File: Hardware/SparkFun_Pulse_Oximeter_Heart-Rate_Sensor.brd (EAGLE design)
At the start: 25.4 x 12.7 mm, 48 parts, among them U1 MAX30101EFD+T, U2 MAX32664GWEA+T, U3 1.8V/100mA, Y1 32.768kHz

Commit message: Moves silk labels around
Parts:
- added U$17: (no value), Pulse:PULSE0
- added U$18: (no value), and:AND0
- added U$19: (no value), SparkFun-Aesthetics:SFE_LOGO_FLAME_.1
- moved U$16 9.56 mm to (19.6, 9.91)
- moved U$14 6.35 mm to (25.7, 10.9)
- moved U$15 6.35 mm to (25.7, 9.91)
- moved U$1 1.05 mm to (24.4, 8.38), turned to 270 degrees
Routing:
- net GND: vias 42 -> 40
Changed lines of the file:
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@@
 <element name="LOGO1" library="SparkFun-Aesthetics" package="SFE_LOGO_FLAME_.1" value="SFE_LOGO_FLAME.1_INCH" x="23.876" y="1.778" smashed="yes"/>
 <element name="LOGO2" library="SparkFun-Aesthetics" package="OSHW-LOGO-MINI" value="OSHW-LOGOMINI" x="21.082" y="1.524" smashed="yes"/>
-<element name="U$1" library="Labels" package="I_SUPER2_C-()-03" value="" x="23.368" y="8.636" smashed="yes" rot="MR0"/>
+<element name="U$1" library="Labels" package="I_SUPER2_C-()-03" value="" x="24.384" y="8.382" smashed="yes" rot="MR270"/>
 <element name="U$3" library="Labels" package="GND-03" value="" x="1.61798125" y="1.267459375" smashed="yes"/>
 <element name="U$4" library="buzzard_labels" package="SCL0" value="" x="1.678940625" y="8.83158125" smashed="yes"/>
@@
 <element name="U$12" library="Labels" package="3V3-03" value="" x="5.67181875" y="3.7846" smashed="yes" rot="MR0"/>
 <element name="U$13" library="Labels" package="3V3-TEXT" value="" x="1.610359375" y="3.84048125" smashed="yes"/>
-<element name="U$14" library="oximeter" package="OXIMETER0" value="" x="25.654" y="4.572" smashed="yes" rot="MR0"/>
-<element name="U$15" library="Heart Rate" package="HEART_RATE0" value="" x="25.654" y="3.556" smashed="yes" rot="MR0"/>
-<element name="U$16" library="Monitor" package="MONITOR0" value="" x="25.654" y="2.54" smashed="yes" rot="MR0"/>
+<element name="U$14" library="oximeter" package="OXIMETER0" value="" x="25.654" y="10.922" smashed="yes" rot="MR0"/>
+<element name="U$15" library="Heart Rate" package="HEART_RATE0" value="" x="25.654" y="9.906" smashed="yes" rot="MR0"/>
+<element name="U$16" library="Monitor" package="MONITOR0" value="" x="19.558" y="9.906" smashed="yes" rot="MR0"/>
 <element name="LOGO3" library="SparkFun-Aesthetics" package="SFE_LOGO_NAME_.1" value="SFE_LOGO_NAME.1_INCH" x="13.208" y="1.778" smashed="yes" rot="MR0"/>
 <element name="FD1" library="SparkFun-Aesthetics" package="FIDUCIAL-MICRO" value="FIDUCIALUFIDUCIAL" x="5.262878125" y="12.082778125" smashed="yes" rot="MR0"/>
@@
 <element name="FD3" library="SparkFun-Aesthetics" package="FIDUCIAL-MICRO" value="FIDUCIALUFIDUCIAL" x="24.638" y="0.762" smashed="yes" rot="MR0"/>
 <element name="FD4" library="SparkFun-Aesthetics" package="FIDUCIAL-MICRO" value="FIDUCIALUFIDUCIAL" x="24.638" y="0.762" smashed="yes"/>
+<element name="U$17" library="Pulse" package="PULSE0" value="" x="25.654" y="11.938" smashed="yes" rot="MR0"/>
+<element name="U$18" library="and" package="AND0" value="" x="20.32" y="10.922" smashed="yes" rot="MR0"/>
+<element name="U$19" library="SparkFun-Aesthetics" package="SFE_LOGO_FLAME_.1" value="" x="6.858" y="4.064" smashed="yes" rot="MR0"/>
 </elements>
 <signals>
@@
 <via x="8.6868" y="9.3472" extent="1-16" drill="0.3048"/>
 <via x="7.6708" y="10.3632" extent="1-16" drill="0.3048"/>
-<via x="5.3848" y="9.8552" extent="1-16" drill="0.3048"/>
+<via x="5.1308" y="9.3472" extent="1-16" drill="0.3048"/>
 <via x="7.7063625" y="5.91058125" extent="1-16" drill="0.1016"/>
-<via x="11.623040625" y="6.301740625" extent="1-16" drill="0.3048"/>
-<via x="14.592303125" y="6.5913" extent="1-16" drill="0.3048"/>
-<via x="15.64894375" y="6.25601875" extent="1-16" drill="0.3048"/>
+<via x="11.673840625" y="6.428740625" extent="1-16" drill="0.3048"/>
+<via x="15.97914375" y="6.25601875" extent="1-16" drill="0.3048"/>
 <via x="15.9740625" y="5.158740625" extent="1-16" drill="0.3048"/>
 <via x="19.6951625" y="8.37438125" extent="1-16" drill="0.3048"/>
@@
 <via x="5.811521875" y="1.25221875" extent="1-16" drill="0.3048"/>
 <via x="8.097521875" y="1.25221875" extent="1-16" drill="0.3048"/>
-<via x="5.1308" y="7.5692" extent="1-16" drill="0.3048"/>
+<via x="5.1308" y="8.0772" extent="1-16" drill="0.3048"/>
 <via x="5.1308" y="6.0452" extent="1-16" drill="0.3048"/>
 <via x="6.1468" y="6.0452" extent="1-16" drill="0.3048"/>
-<via x="4.3688" y="9.3472" extent="1-16" drill="0.3048"/>
-<via x="15.5448" y="2.7432" extent="1-16" drill="0.3048"/>
-<via x="16.5608" y="2.7432" extent="1-16" drill="0.3048"/>
+<via x="14.7828" y="2.7432" extent="1-16" drill="0.3048"/>
+<via x="16.7132" y="2.794" extent="1-16" drill="0.3048"/>
 <via x="13.5128" y="0.7112" extent="1-16" drill="0.3048"/>
 <via x="11.7348" y="0.7112" extent="1-16" drill="0.3048"/>
-<via x="16.4820625" y="4.142740625" extent="1-16" drill="0.3048"/>
+<via x="16.7360625" y="4.142740625" extent="1-16" drill="0.3048"/>
 <via x="14.63294375" y="9.30401875" extent="1-16" drill="0.3048"/>
 <via x="15.4787625" y="8.64361875" extent="1-16" drill="0.3048"/>
 <via x="17.42694375" y="10.82801875" extent="1-16" drill="0.3048"/>
 <via x="18.18894375" y="12.09801875" extent="1-16" drill="0.3048"/>
-<via x="22.25294375" y="12.09801875" extent="1-16" drill="0.3048"/>
-<via x="22.25294375" y="11.08201875" extent="1-16" drill="0.3048"/>
 <via x="24.03094375" y="7.01801875" extent="1-16" drill="0.3048"/>
 <via x="24.03094375" y="3.46201875" extent="1-16" drill="0.3048"/>
@@
 <via x="4.287521875" y="1.25221875" extent="1-16" drill="0.3048"/>
 <via x="3.525521875" y="2.52221875" extent="1-16" drill="0.3048"/>
-<via x="13.0048" y="11.3792" extent="1-16" drill="0.3048"/>
 <via x="17.5768" y="9.6012" extent="1-16" drill="0.3048"/>
 <via x="16.837665625" y="0.840740625" extent="1-16" drill="0.3048"/>
 <via x="18.107665625" y="0.840740625" extent="1-16" drill="0.3048"/>
 <via x="3.3528" y="11.1252" extent="1-16" drill="0.3048"/>
-<via x="12.722859375" y="10.4267" extent="1-16" drill="0.3048"/>
-<via x="12.186921875" y="6.7183" extent="1-16" drill="0.3048"/>
-<via x="13.576303125" y="6.5913" extent="1-16" drill="0.3048"/>
+<via x="14.211303125" y="6.6421" extent="1-16" drill="0.3048"/>
 <wire x1="7.706" y1="5.914" x2="7.7063625" y2="5.9136375" width="0.2032" layer="1"/>
 <wire x1="7.7063625" y1="5.9136375" x2="7.7063625" y2="5.91058125" width="0.2032" layer="1"/>
+<via x="11.4554" y="2.54" extent="1-16" drill="0.3048"/>
+<via x="12.9794" y="2.54" extent="1-16" drill="0.3048"/>
+<via x="18.9331625" y="6.08838125" extent="1-16" drill="0.3048"/>
+<via x="18.9331625" y="4.31038125" extent="1-16" drill="0.3048"/>
+<via x="22.25294375" y="12.09801875" extent="1-16" drill="0.3048"/>
 </signal>
 <signal name="N$2">
@@
 <wire x1="12.192" y1="6.0198" x2="12.192" y2="5.088" width="0.254" layer="1"/>
 <wire x1="12.192" y1="5.088" x2="12.2" y2="5.08" width="0.254" layer="1"/>
-<wire x1="12.2" y1="5.08" x2="12.2" y2="3.8434" width="0.2032" layer="1"/>
-<wire x1="12.2" y1="3.8434" x2="11.9634" y2="3.6068" width="0.2032" layer="1"/>
-<wire x1="11.9634" y1="3.6068" x2="10.2489" y2="3.6068" width="0.2032" layer="1"/>
-<wire x1="10.2489" y1="3.6068" x2="9.916159375" y2="3.939540625" width="0.2032" layer="1"/>
+<wire x1="12.2" y1="5.08" x2="12.2" y2="3.8434" width="0.254" layer="1"/>
+<wire x1="12.2" y1="3.8434" x2="11.99388125" y2="3.63728125" width="0.254" layer="1"/>
+<wire x1="11.99388125" y1="3.63728125" x2="10.21841875" y2="3.63728125" width="0.254" layer="1"/>
+<wire x1="10.21841875" y1="3.63728125" x2="9.916159375" y2="3.939540625" width="0.254" layer="1"/>
 <via x="9.916159375" y="3.939540625" extent="1-16" drill="0.254"/>
 <wire x1="1.27" y1="3.81" x2="3.235959375" y2="3.81" width="0.254" layer="16"/>

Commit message: Pushes temp lib to SparkFun Eagle Libraries and replaces parts in design with those parts
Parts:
- U1: value MAX30101EFD+T -> MAX30101EFD; device temp:14_PIN_OESIP -> SparkFun-IC-Special-Function:14_PIN_OESIP
- U2: value MAX32664GWEA+T -> MAX32664GWEA; device temp:16_PIN_WLP -> SparkFun-IC-Special-Function:16_PIN_WLP
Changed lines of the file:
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@@
 <attribute name="VALUE" x="18.034" y="8.636" size="0.4064" layer="27" rot="R270"/>
 </element>
-<element name="U1" library="temp" package="14_PIN_OESIP" value="MAX30101EFD+T" x="12.7" y="6.604" smashed="yes" rot="MR270">
+<element name="U1" library="SparkFun-IC-Special-Function" package="14_PIN_OESIP" value="MAX30101EFD" x="12.7" y="6.604" smashed="yes" rot="MR270">
 <attribute name="NAME" x="9.490190625" y="9.241540625" size="1" layer="26" rot="MR270"/>
 <attribute name="PROD_ID" value="IC-14270" x="12.7" y="6.604" size="1.778" layer="28" rot="MR270" display="off"/>
 <attribute name="VALUE" x="16.887190625" y="9.241540625" size="1" layer="28" rot="MR270"/>
 </element>
-<element name="U2" library="temp" package="16_PIN_WLP" value="MAX32664GWEA+T" x="7.874" y="6.096" smashed="yes" rot="R90">
+<element name="U2" library="SparkFun-IC-Special-Function" package="16_PIN_WLP" value="MAX32664GWEA" x="7.874" y="6.096" smashed="yes" rot="R90">
 <attribute name="NAME" x="6.656" y="5.304" size="1" layer="25" rot="R90"/>
 <attribute name="PROD_ID" value="IC-14271" x="7.874" y="6.096" size="1.778" layer="27" rot="R90" display="off"/>

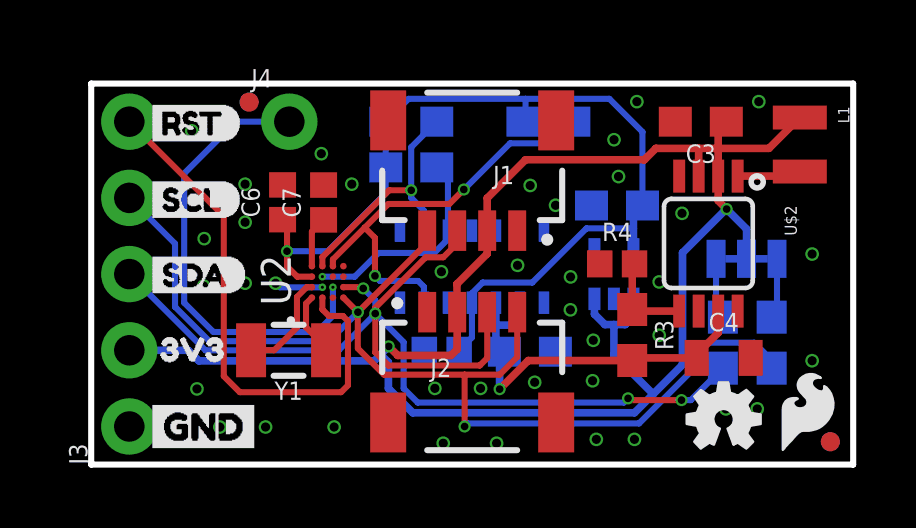
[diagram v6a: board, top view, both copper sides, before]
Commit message: Fixes slik labels on bottom, adjusts traces on Oscillator and reset line, changes ground vias to 10 mil
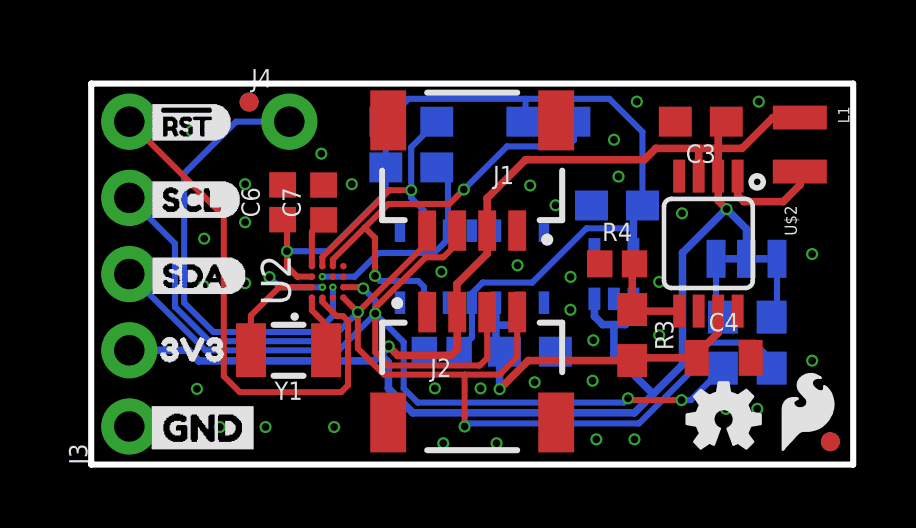
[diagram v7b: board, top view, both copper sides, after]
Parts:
- added U$20: (no value), SDA_TOP:SDA0
- U$10: device buzzard_labels:SCL0 -> SDA:SDA0
- U$5: device SDA:SDA0 -> Labels:GND-03
- U$6: device RST:RST0 -> RST_BAR:#RST0
- U$8: device RST:RST0 -> RST_BOT:#RST0
- U$9: device SDA:SDA0 -> SCL:SCL0
- moved U$5 5.10 mm to (1.60, 1.23)
- moved U$10 4.31 mm to (5.18, 6.31), turned to 0 degrees
- moved U$3 4.26 mm to (5.88, 1.25), flipped to the bottom
- moved U$9 4.15 mm to (5.00, 8.83), turned to 0 degrees
- moved U$8 3.17 mm to (4.82, 11.4), turned to 0 degrees
- moved U$6 0.10 mm to (1.56, 11.4)
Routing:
- net N$3: track 2.14 -> 3.48 mm

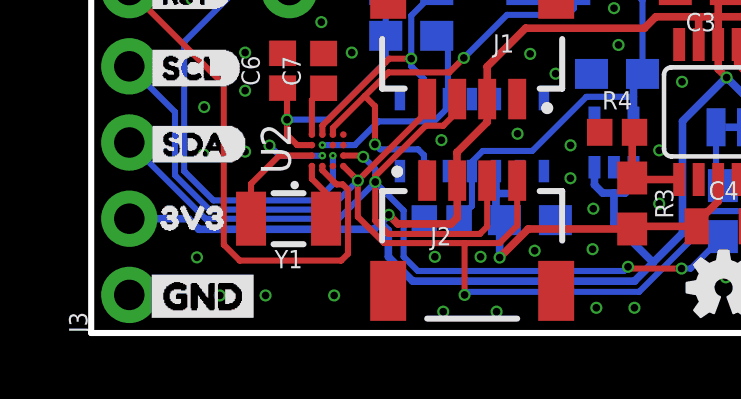
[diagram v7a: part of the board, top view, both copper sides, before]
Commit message: Adds dimensions and special ordering instructions, adds text to MAX30101 that lists voltage ranges and I2C addresses
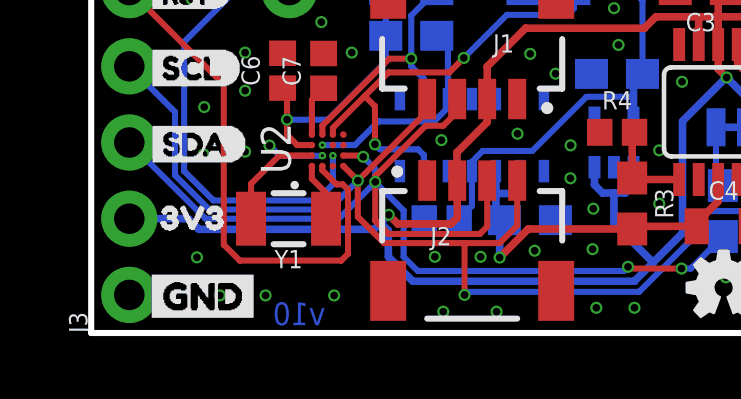
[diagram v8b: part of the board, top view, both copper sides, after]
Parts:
- added LOGO4: SPECIAL_INSTRUCTIONS-ORDERING, SparkFun-Aesthetics:ORDERING_INSTRUCTIONS
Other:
- board text added: "Measurments in Inches"
- board text added: "Via on Pad for small BGA"
- board text added: "v10"
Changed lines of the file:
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@@
 <layer number="44" name="Drills" color="7" fill="1" visible="no" active="yes"/>
 <layer number="45" name="Holes" color="7" fill="1" visible="yes" active="yes"/>
-<layer number="46" name="Milling" color="3" fill="1" visible="no" active="yes"/>
-<layer number="47" name="Measures" color="7" fill="1" visible="no" active="yes"/>
+<layer number="46" name="Milling" color="3" fill="1" visible="yes" active="yes"/>
+<layer number="47" name="Measures" color="7" fill="1" visible="yes" active="yes"/>
 <layer number="48" name="Document" color="7" fill="1" visible="no" active="yes"/>
 <layer number="49" name="Reference" color="13" fill="1" visible="yes" active="yes"/>
@@
 <layer number="118" name="Rect_Pads" color="7" fill="1" visible="no" active="no"/>
 <layer number="119" name="PF_Ref" color="31" fill="1" visible="no" active="yes"/>
-<layer number="120" name="WFL_Ref" color="25" fill="1" visible="no" active="yes"/>
+<layer number="120" name="WFL_Ref" color="25" fill="1" visible="yes" active="yes"/>
 <layer number="121" name="_tsilk" color="7" fill="1" visible="no" active="no"/>
 <layer number="122" name="_bsilk" color="7" fill="1" visible="no" active="no"/>
@@
 <wire x1="25.4" y1="0" x2="0" y2="0" width="0.2032" layer="20"/>
 <text x="22.352" y="-10.16" size="1.778" layer="51" font="vector">Elias Santistevan</text>
+<text x="7.807959375" y="0.25908125" size="0.762" layer="16" font="vector" ratio="15" rot="MR0">v10</text>
+<text x="-23.368" y="-25.4" size="2.032" layer="51" font="vector">Via on Pad for small BGA</text>
+<dimension x1="25.4" y1="12.7" x2="0" y2="12.7" x3="12.7" y3="18.034" textsize="2.54" textratio="15" layer="47" dtype="horizontal" unit="inch"/>
+<dimension x1="25.4" y1="0" x2="25.4" y2="12.7" x3="32.766" y3="6.35" textsize="2.54" textratio="15" layer="47" dtype="horizontal" unit="inch"/>
+<text x="-1.524" y="23.114" size="2.54" layer="47" font="vector" ratio="15">Measurments in Inches</text>
 </plain>
 <attributes>
@@
 <element name="U$5" library="Labels" package="GND-03" value="" x="1.59511875" y="1.22681875" smashed="yes"/>
 <element name="U$20" library="SDA_TOP" package="SDA0" value="" x="1.68401875" y="6.29411875" smashed="yes"/>
+<element name="LOGO4" library="SparkFun-Aesthetics" package="ORDERING_INSTRUCTIONS" value="SPECIAL_INSTRUCTIONS-ORDERING" x="-24.892" y="-11.43" smashed="yes"/>
 </elements>
 <signals>
